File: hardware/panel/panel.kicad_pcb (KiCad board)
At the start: 2 copper layers, 62 x 104.3 mm, 5 parts

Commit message: Panel: regenerate from Wells's fresh Figma export of the test dot
The Desktop export (airwriter-top.svg) re-serializes the same test-cell
dot that 4a30bd4 already shipped (same centre, same 8px radius) but as
a plain black <circle transform="matrix(...)"> instead of a <path>
filled #111111 -- exactly the encoding 4a30bd4's own commit message
warned about: "the panel pipeline ignores <circle> and only ingests
white/#fff/#111 fills, so a plain black circle would have been
silently dropped." Restored the established path/#111111 encoding for
that one element (identical geometry, verified byte-identical to the
committed panel.svg elsewhere) so svg2poly.py keeps picking it up as
the silk mask-knockout, and reran generate.sh.

panel.svg itself has no diff. Regenerating the board reassigned the
four corner standoffs' MT1-4 labels to a different (geometrically
equivalent) permutation and reset two unrelated KiCad project-file
defaults (pad width, a blank step export path) -- pre-existing
non-determinism in emit_board.py, not from this change. The four
pre-existing test failures in test_floors.py/test_panel_layout.py/
test_svg2poly.py (hole_dia 3.6 vs 3.8, knockout-glyph count, gold-art
y-bound) are unchanged before and after this regen.

Refs: W-801
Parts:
- moved MT3 100.1 mm to (5.64, 91.9)
- moved MT1 98.6 mm to (5.64, 5.64)
- moved MT2 50.7 mm to (56.4, 5.64)
- moved MT4 47.7 mm to (53.4, 91.9)
- renumbered MT4 to MT1, MT1 to MT2, MT2 to MT3, MT3 to MT4
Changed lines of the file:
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@@
+	(footprint "panel:SMT_Standoff_M2.5_D6.0mm"
+		(layer "B.Cu")
+		(at 56.3636 5.6364)
+		(property "Reference" "MT2"
+			(at 0 0 0)
+			(layer "F.SilkS")
+			(hide yes)
+			(effects
+				(font
+					(size 1.27 1.27)
+				)
+			)
+		)
+		(property "Value" "9774030151R"
+			(at 0 0 0)
+			(layer "F.Fab")
+			(hide yes)
+			(effects
+				(font
+					(size 1.27 1.27)
+				)
+			)
+		)
+		(property "Datasheet" ""
+			(at 0 0 0)
+			(layer "F.Fab")
+			(hide yes)
+			(effects
+				(font
+					(size 1.27 1.27)
+				)
+			)
+		)
+		(property "Description" ""
+			(at 0 0 0)
+			(layer "F.Fab")
+			(hide yes)
+			(effects
+				(font
+					(size 1.27 1.27)
+				)
+			)
+		)
+		(attr smd)
+		(duplicate_pad_numbers_are_jumpers no)
+		(pad "" smd circle
+			(at 0 0)
+			(size 6 6)
+			(layers "B.Mask")
+		)
+		(embedded_fonts no)
+		(model "${KICAD10_3DMODEL_DIR}/Mounting_Wuerth.3dshapes/Mounting_Wuerth_WA-SMSI-M2.5_H3mm_9774030151.step"
+			(offset
+				(xyz 0 0 0)
+			)
+			(scale
+				(xyz 1 1 1)
+			)
+			(rotate
+				(xyz 0 0 0)
+			)
+		)
+	)
 	(footprint "panel:SMT_Standoff_M2.5_D6.0mm"
 		(layer "B.Cu")
@@
 			(at 0 0 0)
 			(layer "F.SilkS")
-			(hide yes)
-			(effects
-				(font
-					(size 1.27 1.27)
-				)
-			)
-		)
-		(property "Value" "9774030151R"
-			(at 0 0 0)
-			(layer "F.Fab")
-			(hide yes)
-			(effects
-				(font
-					(size 1.27 1.27)
-				)
-			)
-		)
-		(property "Datasheet" ""
-			(at 0 0 0)
-			(layer "F.Fab")
-			(hide yes)
-			(effects
-				(font
-					(size 1.27 1.27)
-				)
-			)
-		)
-		(property "Description" ""
-			(at 0 0 0)
-			(layer "F.Fab")
-			(hide yes)
-			(effects
-				(font
-					(size 1.27 1.27)
-				)
-			)
-		)
-		(attr smd)
-		(duplicate_pad_numbers_are_jumpers no)
-		(pad "" smd circle
-			(at 0 0)
-			(size 6 6)
-			(layers "B.Mask")
-		)
-		(embedded_fonts no)
-		(model "${KICAD10_3DMODEL_DIR}/Mounting_Wuerth.3dshapes/Mounting_Wuerth_WA-SMSI-M2.5_H3mm_9774030151.step"
-			(offset
-				(xyz 0 0 0)
-			)
-			(scale
-				(xyz 1 1 1)
-			)
-			(rotate
-				(xyz 0 0 0)
-			)
-		)
-	)
-	(footprint "panel:SMT_Standoff_M2.5_D6.0mm"
-		(layer "B.Cu")
-		(at 56.3636 5.6364)
-		(property "Reference" "MT2"
-			(at 0 0 0)
-			(layer "F.SilkS")

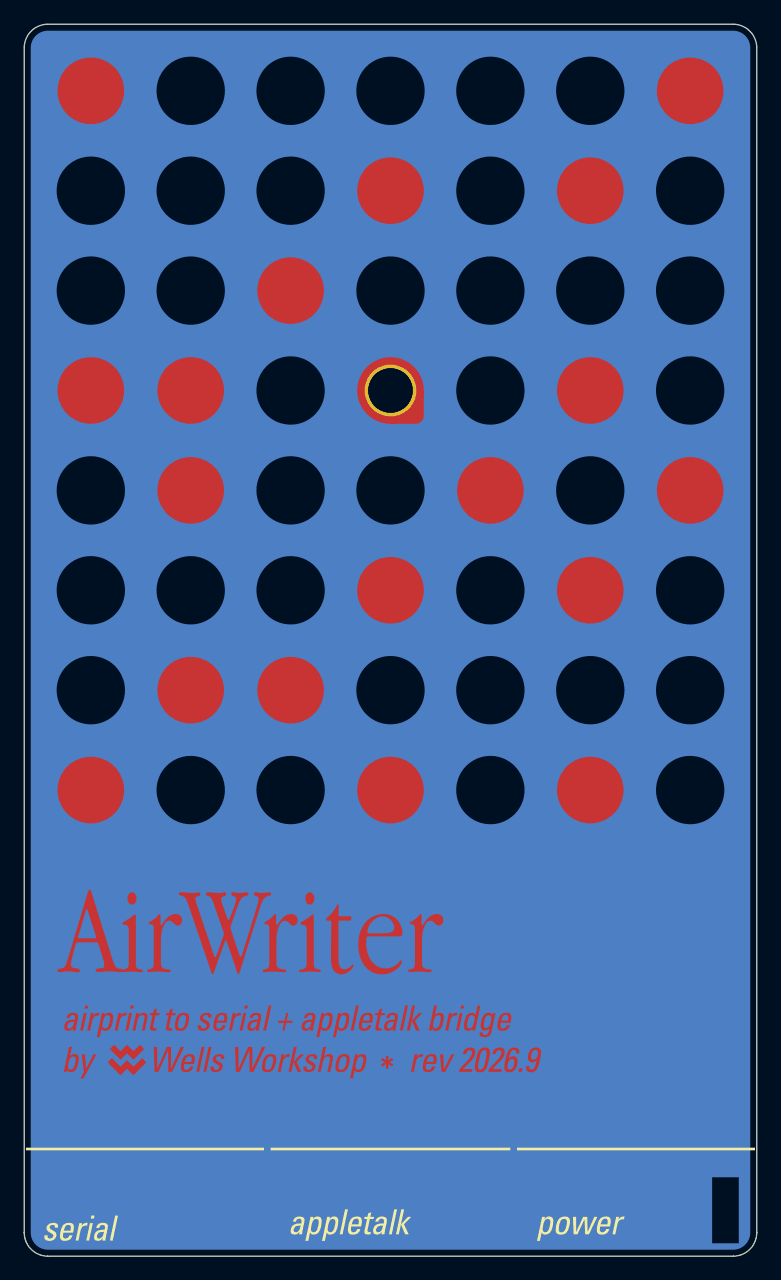
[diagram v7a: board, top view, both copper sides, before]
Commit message: Top case: copper under the front mask, open only where light leaves (W-1091)
Wells: the lit dots look fuzzy. The panel had copper only on its back, so
light came in through each back window, spread sideways in the FR4 and
leaked out through the black mask round the dot; on the 23 teal dots the
mask covers dot and surround alike, so nothing on the front marked the
edge at all. front_flood.py puts the windows in a front flood: teal dots
exactly the dot, bare-FR4 dots and the power slash a hair wider than their
mask openings so misregistration never shows copper. All front copper,
gold art included, is on PANEL_AU so DRC reads one node. Inset 0.55 mm from
the outline, as the back flood. Figma art and dot positions unchanged.

test_front_flood.py: 6 pass. The panel's DRC is as before (4
lib_footprint_issues). generate.sh otherwise reproduces the committed panel
but for the order KiCad 10.0.6 writes the four standoffs in. Four older
panel tests (test_floors x2, test_panel_layout geometry, test_svg2poly)
already fail on the unchanged repo under Python 3.14; left as they were.

Refs: W-1091
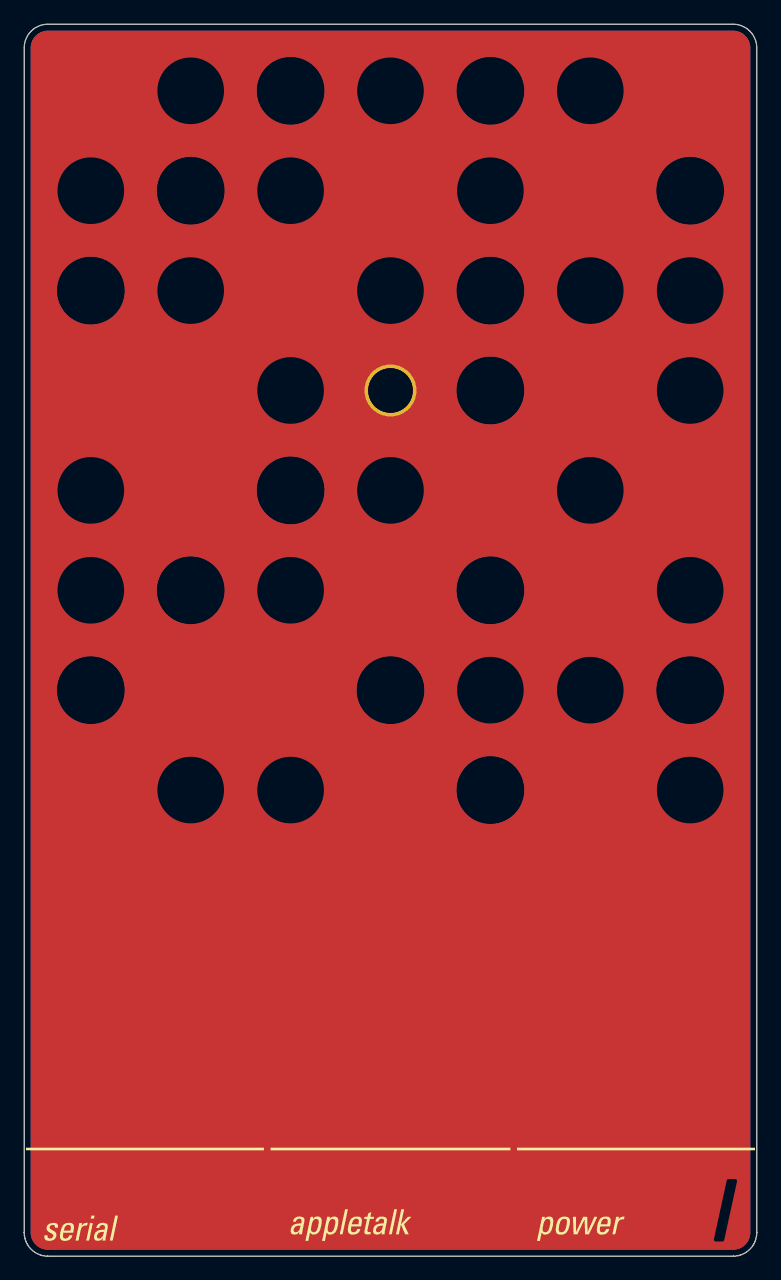
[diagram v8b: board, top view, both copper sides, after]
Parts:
- moved MT2 100.1 mm to (56.4, 5.64)
- moved MT4 98.6 mm to (53.4, 91.9)
- moved MT1 50.7 mm to (5.64, 5.64)
- moved MT3 47.7 mm to (5.64, 91.9)
- renumbered MT2 to MT1, MT3 to MT2, MT4 to MT3, MT1 to MT4
